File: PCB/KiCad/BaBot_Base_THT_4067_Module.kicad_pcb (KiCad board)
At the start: 2 copper layers, 100 x 98.9 mm, 17 parts, among them J1 5V servo power input, J2 TPL0501 H W L, SW1 Momentary NO, U1 CD74HC4067 Module, U15 Red LED 3mm, U2 MIKROE-2332 DIGI POT 2, U3 20-way header to Plate, U4 Arduino Micro A000053

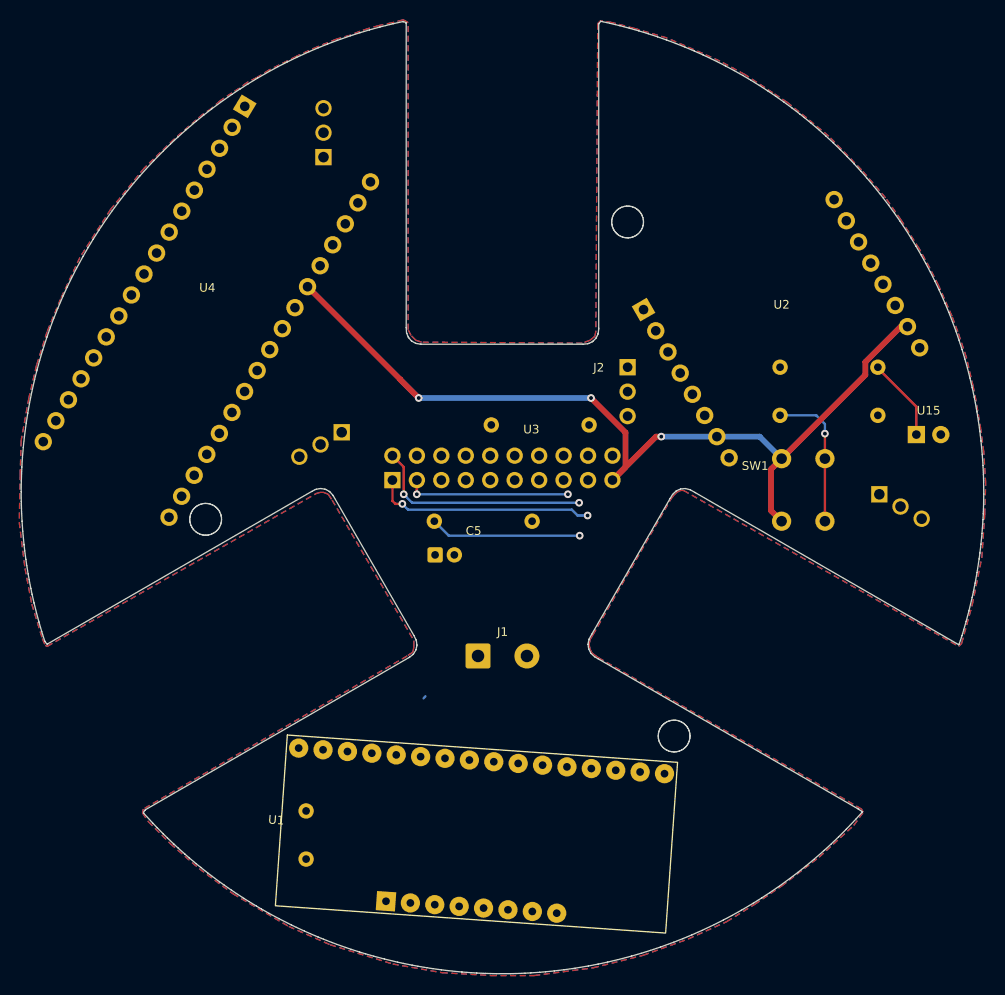
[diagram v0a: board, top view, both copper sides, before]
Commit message: Install trimmer and finish routed four-layer Base
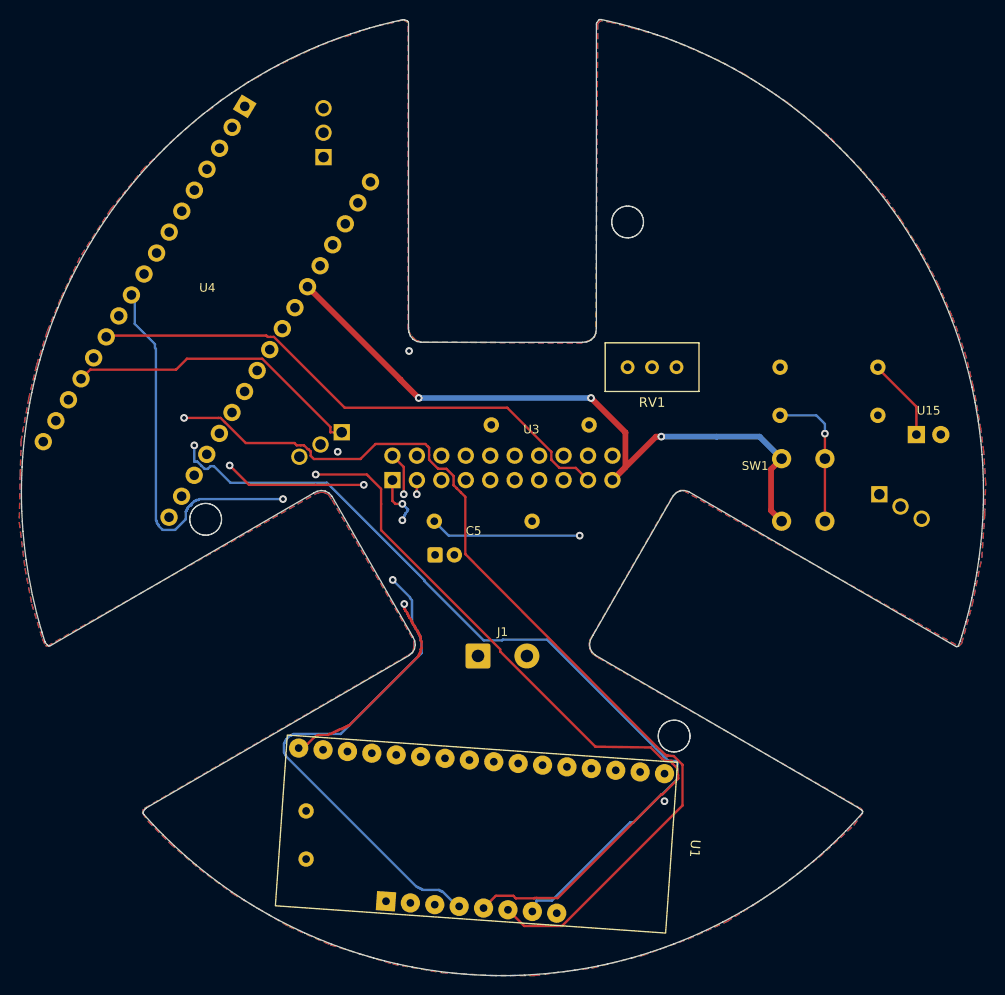
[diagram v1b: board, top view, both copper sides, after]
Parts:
- removed J2: TPL0501 H W L, Header_1x03
- removed U2: MIKROE-2332 DIGI POT 2, DIGI_POT_2_MIKROE2332
- added RV1: 3296W-1-104LF 100k, Potentiometer_THT:Potentiometer_Bourns_3296W_Vertical, F.Cu at (113.0, 87.0)
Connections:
- U4 pad 3: U2_DIN -> (no net)
- U4 pad 4: U2_SCLK -> (no net)
- U4 pad 9: U2_CS -> (no net)
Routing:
- net +5V_SERVO: track 0.00 -> 144.6 mm
- net LED_CONTROL: track 0.00 -> 123.8 mm, vias 0 -> 1
- net U1_S2: track 0.00 -> 114.7 mm, vias 0 -> 1
- net U1_S0: track 0.00 -> 111.4 mm, vias 0 -> 2
- net U1_SIG: track 0.00 -> 104.6 mm
- net U1_S3: track 0.00 -> 104.0 mm, vias 0 -> 1
- net U1_S1: track 0.00 -> 100.3 mm, vias 0 -> 1
- net SERVOB: track 0.00 -> 93.5 mm, vias 0 -> 2
- net +5V_LOGIC: track 92.2 -> 156.1 mm
- net BUTTON: track 15.1 -> 78.5 mm, vias 1 -> 2
- net U1_EN: track 15.7 -> 76.9 mm, vias 1 -> 2
- net IR_LED_CONTROL: track 0.00 -> 56.8 mm
- net SERVOA: track 0.00 -> 39.8 mm
- net PT15: track 0.00 -> 38.5 mm
- net PT13: track 0.00 -> 36.0 mm
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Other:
- board size 100 x 98.9 mm -> 100 x 99.3 mm
- copper layers 2 -> 4
